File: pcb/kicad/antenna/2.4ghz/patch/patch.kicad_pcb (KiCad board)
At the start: 2 copper layers, 1 part, among them P1 CONN_01X02

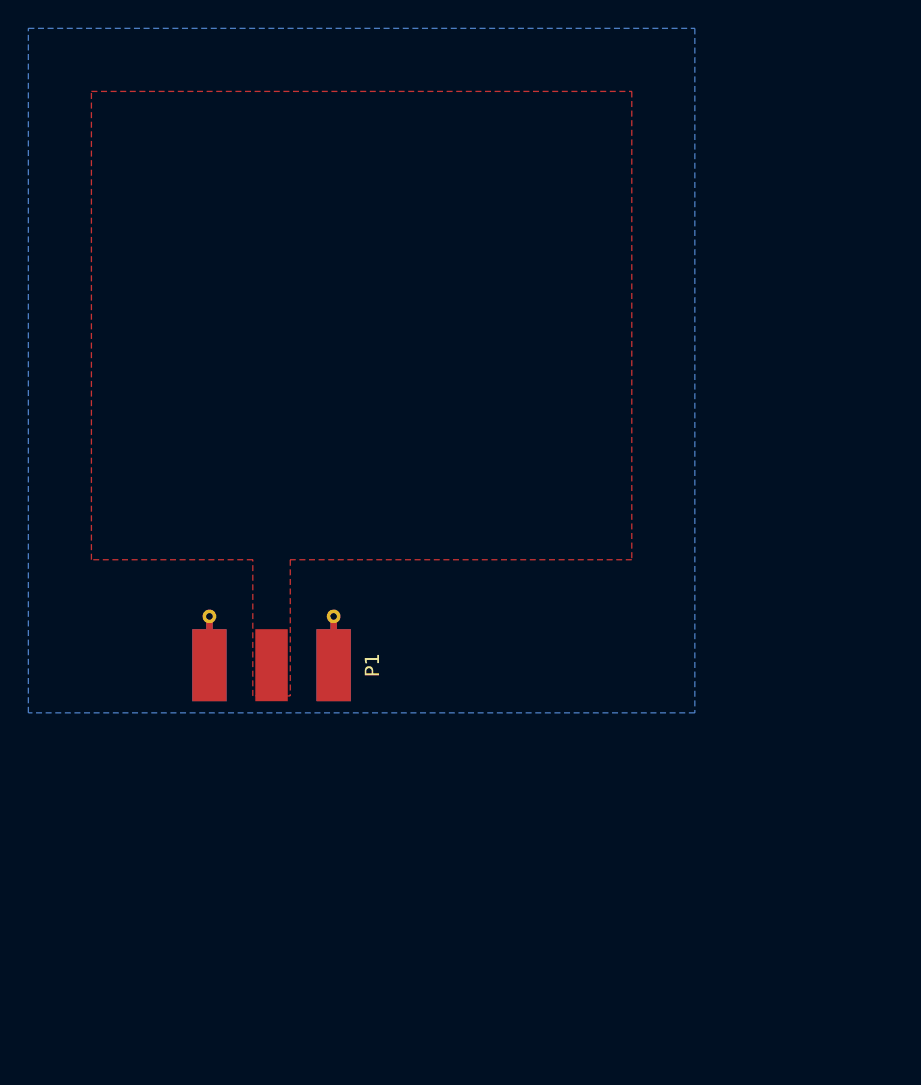
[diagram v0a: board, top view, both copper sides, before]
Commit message: Add new revision for patch antenna
New revision shrinks the first revision patch antenna dimensions to
achieve a higher resonance frequency. Feedline was moved closer to the
center to lower the characteristic impedance. The SMA footprint was
edited to remove error with unconnected thermal relief. Layout for the
antenna was simplified with the footprint creator.
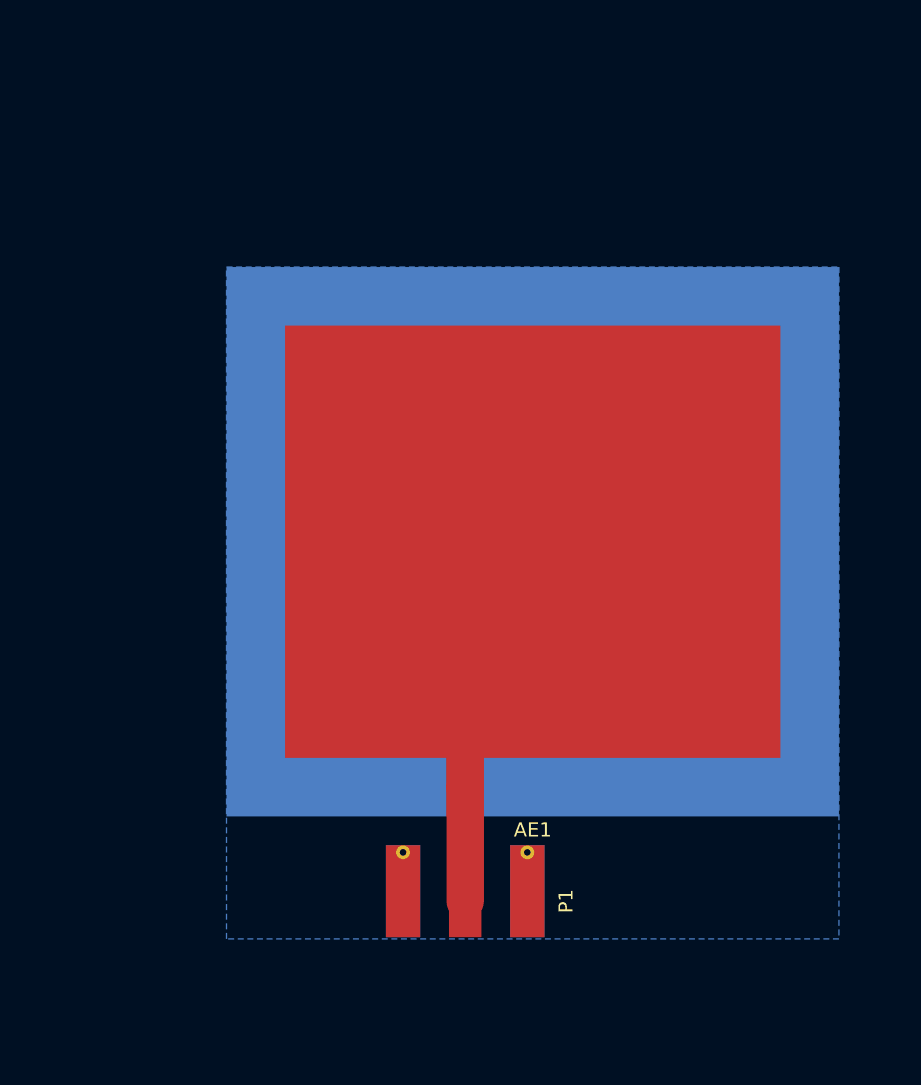
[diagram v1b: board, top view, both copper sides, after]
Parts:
- added AE1: Antenna, Antennas:Patch_Antenna_2.4GHz, F.Cu at (148.6, 88.9)
- P1: value CONN_01X02 -> SMA; footprint Connectors_Molex:Molex_SMA_Jack_Edge_Mount -> Misc:Molex_SMA_Jack_Edge_Mount
- moved P1 21.5 mm to (143.8, 112.5)
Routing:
- net /SIG: track 0.00 -> 27.3 mm
- removed copper zone on F.Cu, net /SIG
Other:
- net class Default: clearance 0.254 -> 0.127; trace_width 0.127 -> 2.6416; via_dia 0.3556 -> 0.3048
- rule trace_clearance: 0.254 -> 0.127
- board text added: "0.2"
- board text added: "March 15, 2017"
- board text removed: "0.1"
- board text removed: "February 15, 2017"
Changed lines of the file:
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@@
 (kicad_pcb (version 4) (host pcbnew 4.0.5)
   (general
-    (links 9)
-    (no_connects 4)
-    (area 112.929999 52.604999 272.295714 194.39)
+    (links 8)
+    (no_connects 0)
+    (area 126.873 67.678 272.295714 194.39)
     (thickness 1.5748)
     (drawings 7)
-    (tracks 0)
+    (tracks 3)
     (zones 0)
-    (modules 1)
+    (modules 2)
     (nets 3)
   )
@@
   )
   (setup
-    (last_trace_width 0.127)
-    (trace_clearance 0.254)
-    (zone_clearance 0.508)
+    (last_trace_width 2.6416)
+    (trace_clearance 0.127)
+    (zone_clearance 0.127)
     (zone_45_only yes)
     (trace_min 0.127)
     (segment_width 0.2)
     (edge_width 0.15)
-    (via_size 0.3556)
+    (via_size 0.3048)
     (via_drill 0.254)
     (via_min_size 0.254)
@@
     (mod_text_size 1 1)
     (mod_text_width 0.15)
-    (pad_size 1.524 1.524)
-    (pad_drill 0.762)
+    (pad_size 43.18 38.735)
+    (pad_drill 0)
     (pad_to_mask_clearance 0.2)
-    (aux_axis_origin 113.03 100.965)
-    (grid_origin 125.73 94.615)
+    (aux_axis_origin 127 116.9035)
     (visible_elements 7FFFFFFF)
     (pcbplotparams
-      (layerselection 0x030f0_80000001)
+      (layerselection 0x020f0_80000001)
       (usegerberextensions false)
       (excludeedgelayer true)
-      (linewidth 0.100000)
+      (linewidth 0.025400)
       (plotframeref false)
       (viasonmask false)
       (mode 1)
-      (useauxorigin false)
+      (useauxorigin true)
       (hpglpennumber 1)
       (hpglpenspeed 20)
@@
       (drillshape 0)
       (scaleselection 1)
-      (outputdirectory ""))
+      (outputdirectory artwork/))
   )
   (net 0 "")
@@
   (net 2 GND)
   (net_class Default "This is the default net class."
-    (clearance 0.254)
-    (trace_width 0.127)
-    (via_dia 0.3556)
+    (clearance 0.127)
+    (trace_width 2.6416)
+    (via_dia 0.3048)
     (via_drill 0.254)
     (uvia_dia 0.2032)
@@
     (add_net GND)
   )
-  (module Connectors_Molex:Molex_SMA_Jack_Edge_Mount (layer F.Cu)
-    (at 130.175 95.885 90)
-    (descr "Molex SMA Jack, Edge Mount, http://www.molex.com/pdm_docs/sd/732511150_sd.pdf")
+  (module Antennas:Patch_Antenna_2.4GHz (layer F.Cu)
+    (at 148.59 88.9)
+    (descr "2.4GHz Patch Antenna")
+    (tags "antenna patch 2.4")
+    (fp_text reference AE1 (at 0 20.32) (layer F.SilkS)
+      (effects (font (size 1 1) (thickness 0.15)))
+    )
+    (fp_text value Antenna (at 0 -20.32) (layer F.Fab)
+      (effects (font (size 1 1) (thickness 0.15)))
+    )
+    (pad 2 smd rect (at 0 0) (size 43.18 38.735) (layers B.Cu)
+      (net 2 GND))
+    (pad 1 smd rect (at 0 0) (size 34.925 30.48) (layers F.Cu)
+      (net 1 /SIG))
+    (pad 1 smd rect (at -4.7625 17.30375) (size 2.6416 4.1275) (layers F.Cu)
+      (net 1 /SIG))
+  )
+  (module Misc:Molex_SMA_Jack_Edge_Mount (layer F.Cu)
+    (at 143.8275 112.522 90)
+    (descr "Molex SMA Jack, Edge Mount")
     (tags "sma edge")
     (attr smd)
@@
       (effects (font (size 1 1) (thickness 0.15)))
     )
-    (fp_text value CONN_01X02 (at -1.72 -7.11 90) (layer F.Fab)
+    (fp_text value SMA (at -1.72 -7.11 90) (layer F.Fab)
       (effects (font (size 1 1) (thickness 0.15)))
     )
@@
     (pad 1 smd rect (at -1.72 0 90) (size 5.08 2.29) (layers F.Cu F.Paste F.Mask)
       (net 1 /SIG))
-    (pad 2 smd rect (at -1.72 -4.38 90) (size 5.08 2.42) (layers F.Cu F.Paste F.Mask)
+    (pad 2 smd rect (at -1.02 -4.38 90) (size 6.48 2.42) (layers F.Cu F.Paste F.Mask)
       (net 2 GND))
-    (pad 2 smd rect (at -1.72 4.38 90) (size 5.08 2.42) (layers F.Cu F.Paste F.Mask)
+    (pad 2 smd rect (at -1.02 4.38 90) (size 6.48 2.42) (layers F.Cu F.Paste F.Mask)
       (net 2 GND))
-    (pad 2 smd rect (at -1.72 -4.38 90) (size 5.08 2.42) (layers B.Cu B.Paste B.Mask)
+    (pad 2 smd rect (at -1.02 -4.38 90) (size 6.48 2.42) (layers B.Cu B.Paste B.Mask)
       (net 2 GND))
-    (pad 2 smd rect (at -1.72 4.38 90) (size 5.08 2.42) (layers B.Cu B.Paste B.Mask)
+    (pad 2 smd rect (at -1.02 4.38 90) (size 6.48 2.42) (layers B.Cu B.Paste B.Mask)
       (net 2 GND))
     (pad 2 thru_hole circle (at 1.72 -4.38 90) (size 0.97 0.97) (drill 0.46) (layers *.Cu)
@@
     (pad 2 thru_hole circle (at 1.72 4.38 90) (size 0.97 0.97) (drill 0.46) (layers *.Cu)
       (net 2 GND))
-    (pad 2 smd rect (at 1.27 -4.38 90) (size 0.89 0.46) (layers F.Cu)
-      (net 2 GND))
-    (pad 2 smd rect (at 1.27 4.38 90) (size 0.89 0.46) (layers F.Cu)
-      (net 2 GND))
-    (pad 2 smd rect (at 1.27 -4.38 90) (size 0.89 0.46) (layers B.Cu)
-      (net 2 GND))
-    (pad 2 smd rect (at 1.27 4.38 90) (size 0.89 0.46) (layers B.Cu)
-      (net 2 GND))
   )
-  (gr_line (start 160.02 100.965) (end 113.03 100.965) (angle 90) (layer Margin) (width 0.2))
-  (gr_line (start 160.02 52.705) (end 160.02 100.965) (angle 90) (layer Margin) (width 0.2))
-  (gr_line (start 113.03 52.705) (end 160.02 52.705) (angle 90) (layer Margin) (width 0.2))
-  (gr_line (start 113.03 100.965) (end 113.03 52.705) (angle 90) (layer Margin) (width 0.2))
-  (gr_text "February 15, 2017" (at 217.17 193.04) (layer Cmts.User)
+  (gr_line (start 170.18 69.5325) (end 127 69.5325) (angle 90) (layer Margin) (width 0.2))
+  (gr_line (start 170.18 116.9035) (end 170.18 69.5325) (angle 90) (layer Margin) (width 0.2))
+  (gr_line (start 127 116.9035) (end 170.18 116.9035) (angle 90) (layer Margin) (width 0.2))
+  (gr_line (start 127 69.5325) (end 127 116.9035) (angle 90) (layer Margin) (width 0.2))
+  (gr_text "March 15, 2017" (at 217.17 193.04) (layer Cmts.User)
     (effects (font (size 1.5 1.5) (thickness 0.3)))
   )
-  (gr_text 0.1 (at 270.51 193.04) (layer Cmts.User)
+  (gr_text 0.2 (at 270.51 193.04) (layer Cmts.User)
     (effects (font (size 1.5 1.5) (thickness 0.3)))
   )
@@
     (effects (font (size 1.5 1.5) (thickness 0.3)))
   )
-  (zone (net 2) (net_name GND) (layer B.Cu) (hatch full 0.508)
-    (connect_pads (clearance 0.508))
-    (min_thickness 0.254)
-    (fill yes (arc_segments 16) (thermal_gap 0.508) (thermal_bridge_width 0.508))
+  (segment (start 143.8275 106.20375) (end 143.8275 93.6625) (width 2.6416) (layer F.Cu) (net 1) (status 30))
+  (segment (start 143.8275 93.6625) (end 148.59 88.9) (width 2.6416) (layer F.Cu) (net 1) (status 30))
+  (segment (start 143.8275 114.242) (end 143.8275 106.20375) (width 2.6416) (layer F.Cu) (net 1) (status 30))
+  (zone (net 2) (net_name GND) (layer B.Cu) (hatch edge 0.508)
+    (connect_pads thru_hole_only (clearance 0.127))
+    (min_thickness 0.127)
+    (fill yes (arc_segments 32) (thermal_gap 0.508) (thermal_bridge_width 0.508))
     (polygon
       (pts
-        (xy 113.03 52.705) (xy 160.02 52.705) (xy 160.02 100.965) (xy 113.03 100.965)
+        (xy 170.18 116.9035) (xy 127 116.9035) (xy 127 69.5325) (xy 170.18 69.5325)
       )
     )
-  )
-  (zone (net 1) (net_name /SIG) (layer F.Cu) (hatch full 0.508)
-    (priority 1)
-    (connect_pads (clearance 0.254))
-    (min_thickness 0.254)
-    (fill yes (arc_segments 16) (thermal_gap 0.508) (thermal_bridge_width 0.508))
-    (polygon
-      (pts
-        (xy 128.8542 90.17) (xy 117.475 90.17) (xy 117.475 57.15) (xy 155.575 57.15) (xy 155.575 90.17)
-        (xy 131.4958 90.17) (xy 131.4958 99.7712) (xy 128.8542 99.7712)
-      )
-    )

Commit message: Add alt version of patch antenna with balun
Copied rev0.2 patch antenna and placed a balun in between the SMA link
and the antenna feed. Standardize test board size between the balun and
non-balun designs. Balun balanced feed is questionable; currently placed
to ground. Also changed SMA connector via to have no thermal reliefs.
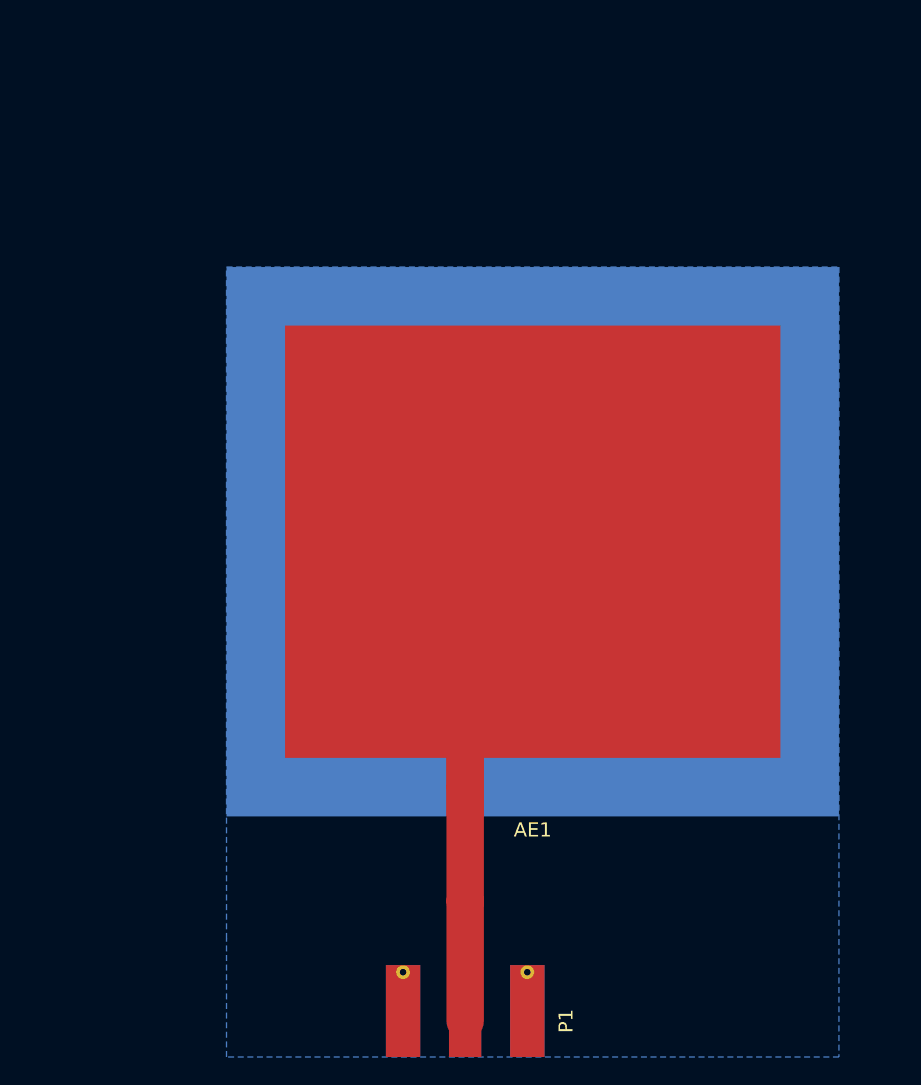
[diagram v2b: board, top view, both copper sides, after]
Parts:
- moved P1 8.45 mm to (143.8, 121.0)
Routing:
- net /SIG: track 27.3 -> 35.8 mm
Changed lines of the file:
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@@
     (thickness 1.5748)
     (drawings 7)
-    (tracks 3)
+    (tracks 4)
     (zones 0)
     (modules 2)
@@
     (pad_drill 0)
     (pad_to_mask_clearance 0.2)
-    (aux_axis_origin 127 116.9035)
+    (aux_axis_origin 127 125.22962)
     (visible_elements 7FFFFFFF)
     (pcbplotparams
@@
   )
   (module Misc:Molex_SMA_Jack_Edge_Mount (layer F.Cu)
-    (at 143.8275 112.522 90)
+    (at 143.8275 120.97004 90)
     (descr "Molex SMA Jack, Edge Mount")
     (tags "sma edge")
@@
       (net 2 GND))
     (pad 2 thru_hole circle (at 1.72 -4.38 90) (size 0.97 0.97) (drill 0.46) (layers *.Cu)
-      (net 2 GND))
+      (net 2 GND) (zone_connect 2))
     (pad 2 thru_hole circle (at 1.72 4.38 90) (size 0.97 0.97) (drill 0.46) (layers *.Cu)
-      (net 2 GND))
+      (net 2 GND) (zone_connect 2))
   )
   (gr_line (start 170.18 69.5325) (end 127 69.5325) (angle 90) (layer Margin) (width 0.2))
-  (gr_line (start 170.18 116.9035) (end 170.18 69.5325) (angle 90) (layer Margin) (width 0.2))
-  (gr_line (start 127 116.9035) (end 170.18 116.9035) (angle 90) (layer Margin) (width 0.2))
-  (gr_line (start 127 69.5325) (end 127 116.9035) (angle 90) (layer Margin) (width 0.2))
+  (gr_line (start 170.18 125.22962) (end 170.18 69.5325) (angle 90) (layer Margin) (width 0.2))
+  (gr_line (start 127 125.22962) (end 170.18 125.22962) (angle 90) (layer Margin) (width 0.2))
+  (gr_line (start 127 69.5325) (end 127 125.22962) (angle 90) (layer Margin) (width 0.2))
   (gr_text "March 15, 2017" (at 217.17 193.04) (layer Cmts.User)
     (effects (font (size 1.5 1.5) (thickness 0.3)))
@@
     (effects (font (size 1.5 1.5) (thickness 0.3)))
   )
+  (segment (start 143.8275 122.69004) (end 143.8275 114.242) (width 2.6416) (layer F.Cu) (net 1) (status 400000))
+  (segment (start 143.8275 114.242) (end 143.8275 106.20375) (width 2.6416) (layer F.Cu) (net 1) (status 30))
   (segment (start 143.8275 106.20375) (end 143.8275 93.6625) (width 2.6416) (layer F.Cu) (net 1) (status 30))
   (segment (start 143.8275 93.6625) (end 148.59 88.9) (width 2.6416) (layer F.Cu) (net 1) (status 30))
-  (segment (start 143.8275 114.242) (end 143.8275 106.20375) (width 2.6416) (layer F.Cu) (net 1) (status 30))
   (zone (net 2) (net_name GND) (layer B.Cu) (hatch edge 0.508)
     (connect_pads thru_hole_only (clearance 0.127))
@@
     (polygon
       (pts
-        (xy 170.18 116.9035) (xy 127 116.9035) (xy 127 69.5325) (xy 170.18 69.5325)
+        (xy 170.18 125.22962) (xy 127 125.22962) (xy 127 116.9035) (xy 127 69.5325) (xy 170.18 69.5325)
       )
     )
+    (polygon
+      (pts        (xy 127 116.9035) (xy 127.00508 116.9162) (xy 127.00508 116.9035)
+      )
+    )
